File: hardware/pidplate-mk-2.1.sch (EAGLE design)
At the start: 41 parts, among them J1 M06X2PTH, Q1 2N7000, Q2 2N3904, U1 ATMEGA328P, U3 VSK-S1, Y1 8MHz

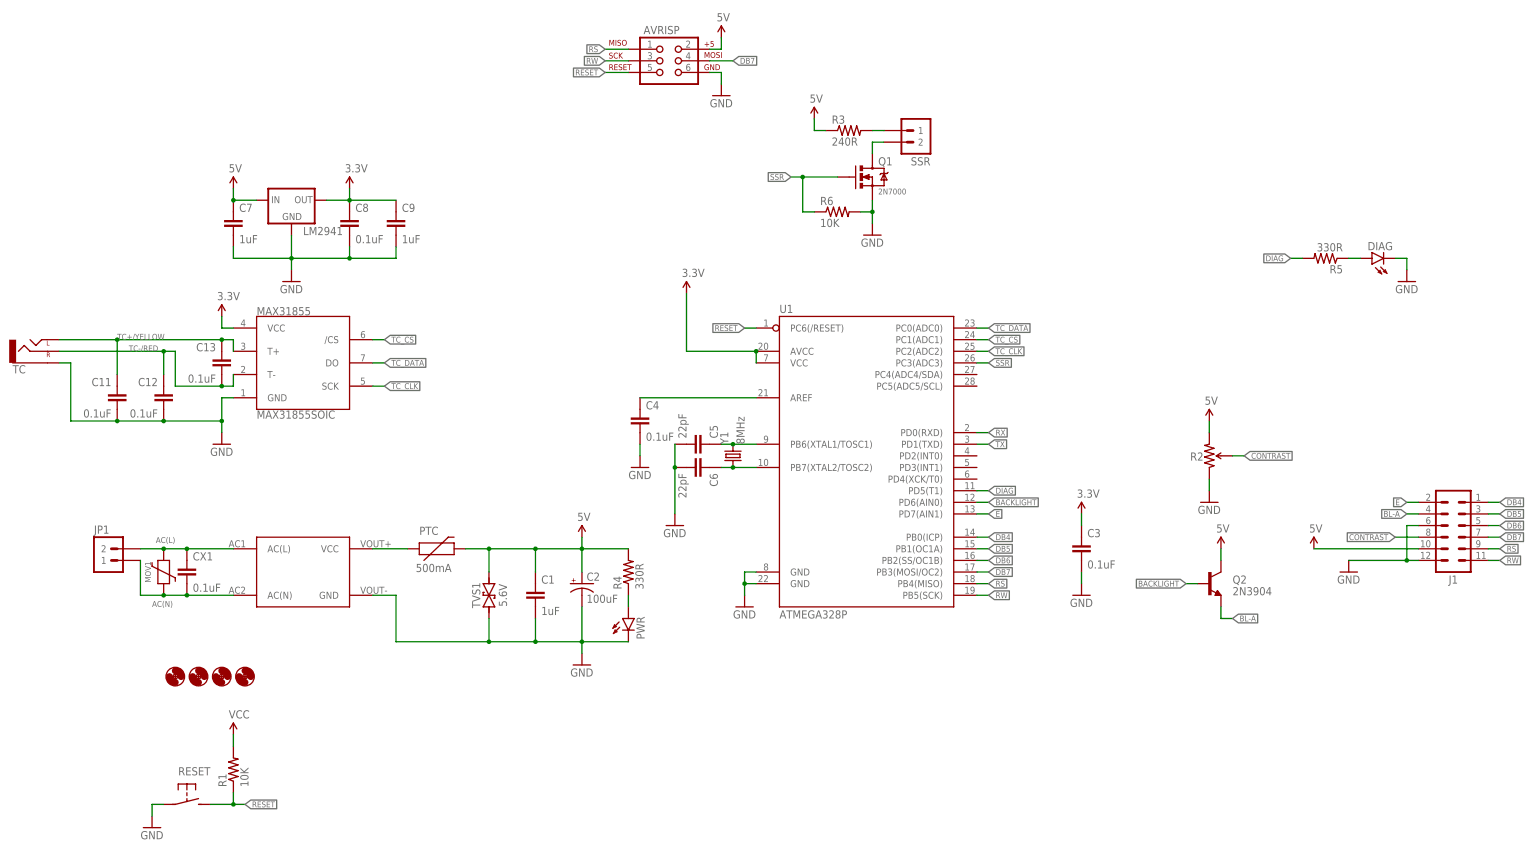
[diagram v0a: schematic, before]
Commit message: revision dos will use 3.3V power to make life easier
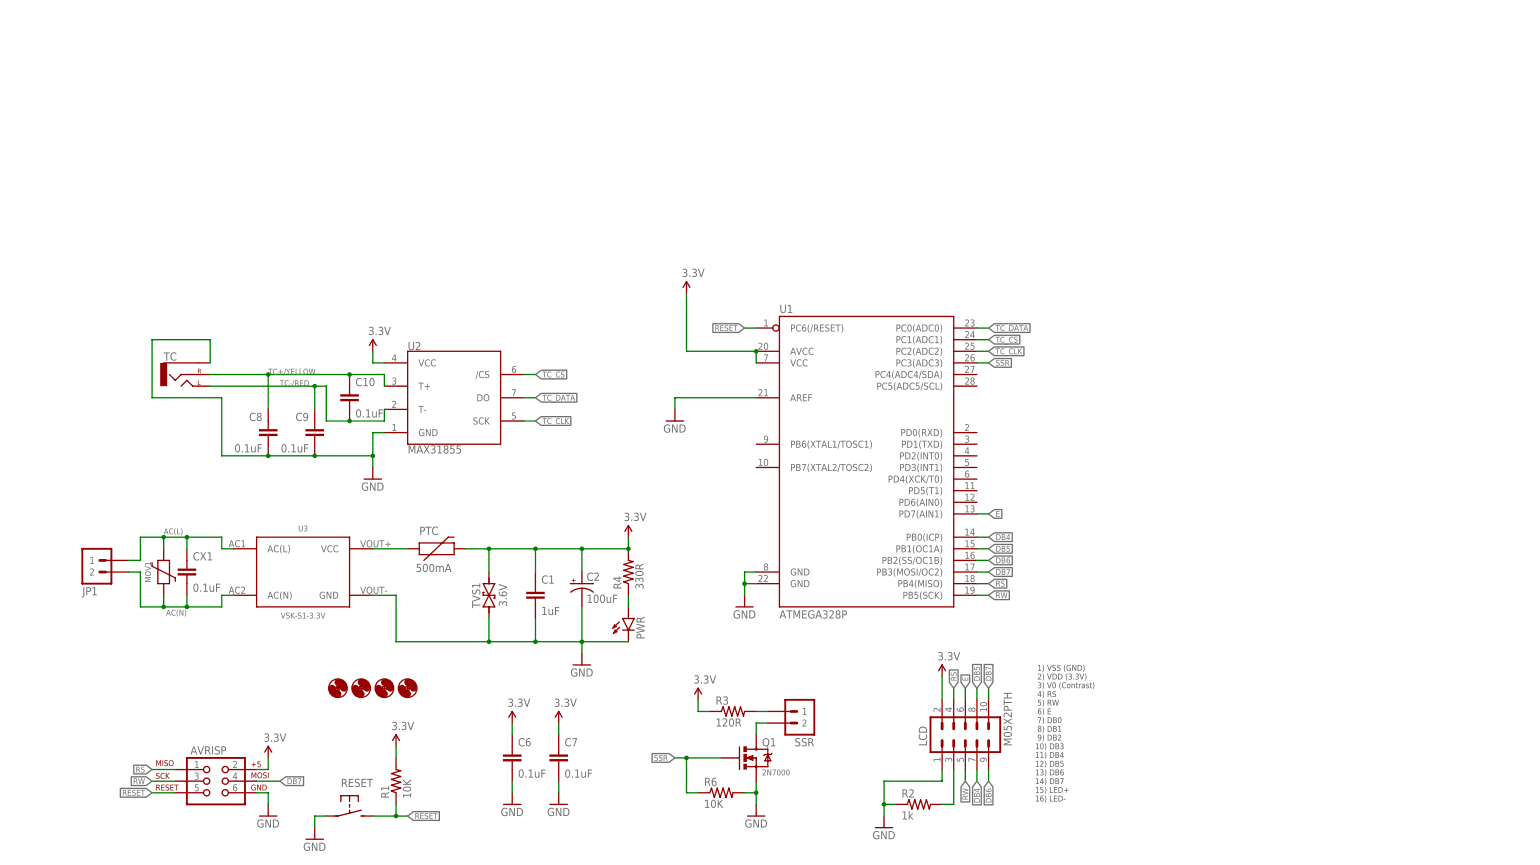
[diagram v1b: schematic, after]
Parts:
- removed C11, C12, C13, C3, C4: 0.1uF, A_butts:CAPACITOR-CERAMIC025-024X044
- removed C5: 22pF, A_butts:CAPACITOR-CERAMIC025-024X044
- removed DIAG: LED3MM, A_butts:LED3MM
- removed J1: M06X2PTH, A_butts:M06X2PTH
- removed LM2941: L2941, A_butts:V_REG_78XXTO-92-INLINE
- removed MAX31855: MAX31855SOIC, A_butts:MAX31855SOIC
- removed Q2: 2N3904, A_butts:TRANSISTOR_NPNTO-92-AMMO-CBE
- removed R5: 330R, A_butts:RESISTORPTH-AXIAL-5.08MM
- removed Y1: 8MHz, A_butts:CRYSTALHC49UV
- added C10: 0.1uF, A_butts:CAPACITOR-CERAMIC025-024X044
- added LCD: M05X2PTH, A_butts:M05X2PTH
- added U2: MAX31855, A_butts:MAX31855SOIC
- C6: value 22pF -> 0.1uF
- C7, C9: value 1uF -> 0.1uF
- R1, R4: device A_butts:RESISTORPTH-AXIAL-5.08MM -> A_butts:RESISTORPTH-AXIAL-6.35MM
- R2: value 20K -> 1k; device A_butts:TRIMPOTPTH -> A_butts:RESISTORPTH-AXIAL-6.35MM
- R3: value 240R -> 120R
- RESET: value SPST-NO-TACT3MM-RA -> SPST-NO-TACT3MM-PTH; device A_butts:SPST-NO-TACT3MM-RA -> A_butts:SPST-NO-TACT3MM-PTH
- TVS1: value 5.6V -> 3.6V
- U3: value VSK-S1 -> VSK-S1-3.3V
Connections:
- removed net 5V: AVRISP.2, C1.1, C2.+, C7.1, J1.10, LM2941.IN, PTC.2, Q2.C, R1.2, R2.CW, R3.1, R4.2, TVS1.2
- removed net BACKLIGHT: Q2.B, U1.PD6(AIN0)
- removed net BL-A: J1.4, Q2.E
- removed net CONTRAST: J1.8, R2.WIPER
- removed net DIAG: R5.2, U1.PD5(T1)
- removed net N$3: C6.1, U1.PB7(XTAL2/TOSC2), Y1.1
- removed net N$4: C5.1, U1.PB6(XTAL1/TOSC1), Y1.2
- removed net N$5: C4.1, U1.AREF
- removed net RX: U1.PD0(RXD)
- removed net TX: U1.PD1(TXD)
- net 3.3V: now also AVRISP.2, C1.1, C2.+, C6.1, C7.1, LCD.2, PTC.2, R1.2, R3.1, R4.2, TVS1.2, U2.VCC; no longer C3.1, C8.1, C9.1, LM2941.OUT, MAX31855.VCC
- net AC(L): now also JP1.1; no longer JP1.2
- net AC(N): now also JP1.2; no longer JP1.1
- net DB4: now also LCD.7; no longer J1.1
- net DB5: now also LCD.8; no longer J1.3
- net DB6: now also LCD.9; no longer J1.5
- net DB7: now also LCD.10; no longer J1.7
- net E: now also LCD.6; no longer J1.2
- net GND: now also LCD.1, R2.1, U1.AREF, U2.GND; no longer C11.2, C12.2, C3.2, C4.2, C5.2, DIAG.C, J1.12, J1.6, LM2941.GND, MAX31855.GND, R2.CCW
- net N$2: now also LCD.3, R2.2; no longer DIAG.A, R5.1
- net RS: now also LCD.4; no longer J1.9
- net RW: now also LCD.5; no longer J1.11
- net TC+/YELLOW: now also C10.1, C8.1, TC.RIGHT, U2.T+; no longer C11.1, C13.1, MAX31855.T+, TC.LEFT
- net TC-/RED: now also C10.2, C9.1, TC.LEFT, U2.T-; no longer C12.1, C13.2, MAX31855.T-, TC.RIGHT
- net TC_CLK: now also U2.SCK; no longer MAX31855.SCK
- net TC_CS: now also U2./CS; no longer MAX31855./CS
- net TC_DATA: now also U2.DO; no longer MAX31855.DO
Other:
- note added: "1) VSS (GND) 2) VDD (3.3V) 3) V0 (Contrast) 4) RS 5) RW 6) E 7) DB0 8) DB1 9) DB2 10) DB3 11) DB4 12) DB5 13) DB6 14) DB7 15) LED+ 16) LED-"
- moved on the sheet: AVRISP, C6, C7, C8, C9, JP1, Q1, R1, R3, R6, RESET, SSR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
